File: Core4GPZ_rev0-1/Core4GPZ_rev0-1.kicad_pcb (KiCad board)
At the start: 2 copper layers, 91.4 x 109.2 mm, 41 parts, among them IC1 MAX9926UAEE_V+, M3 MountingHole_3.2mm_M3_DIN965_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, Q1 FGP3440G2-F085, Q2 FGP3440G2-F085, U1 core4, U2 MPX4250

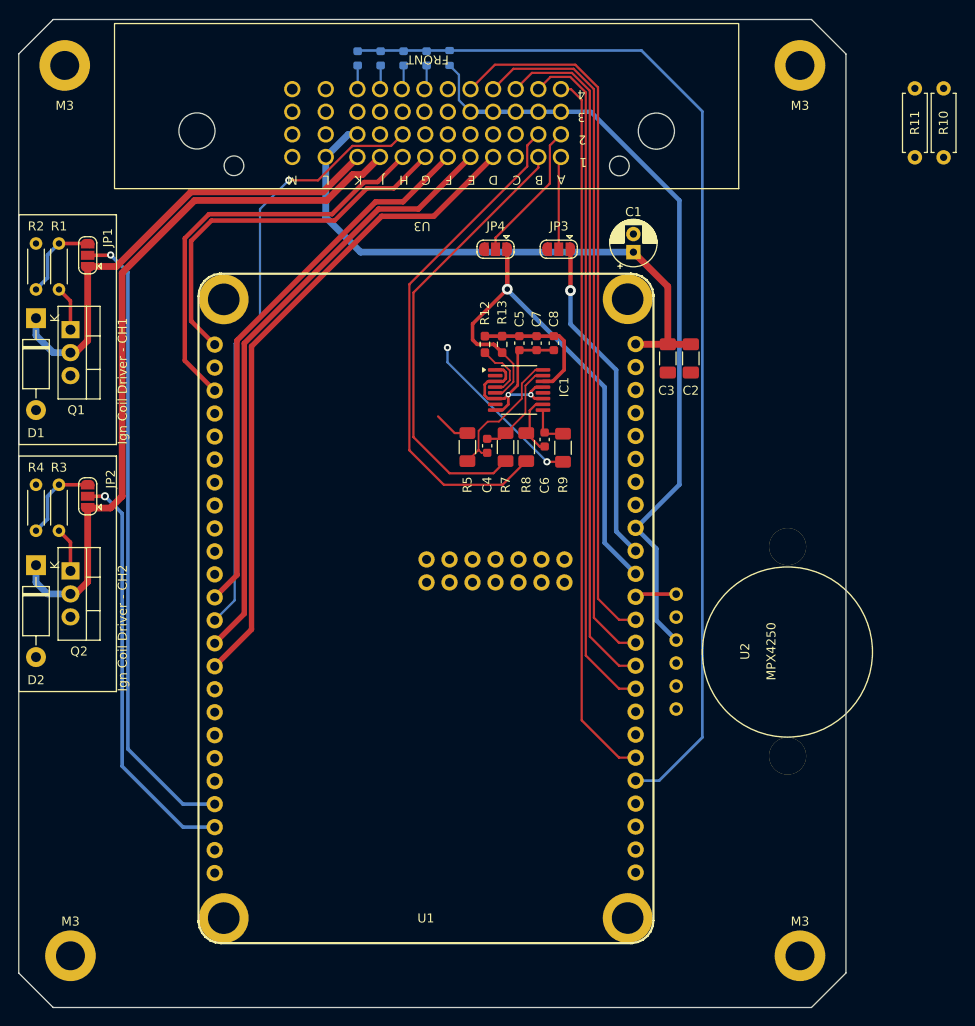
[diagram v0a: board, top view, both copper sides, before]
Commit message: Frist revision
First revision finished, optimised routing, board turned 180°.
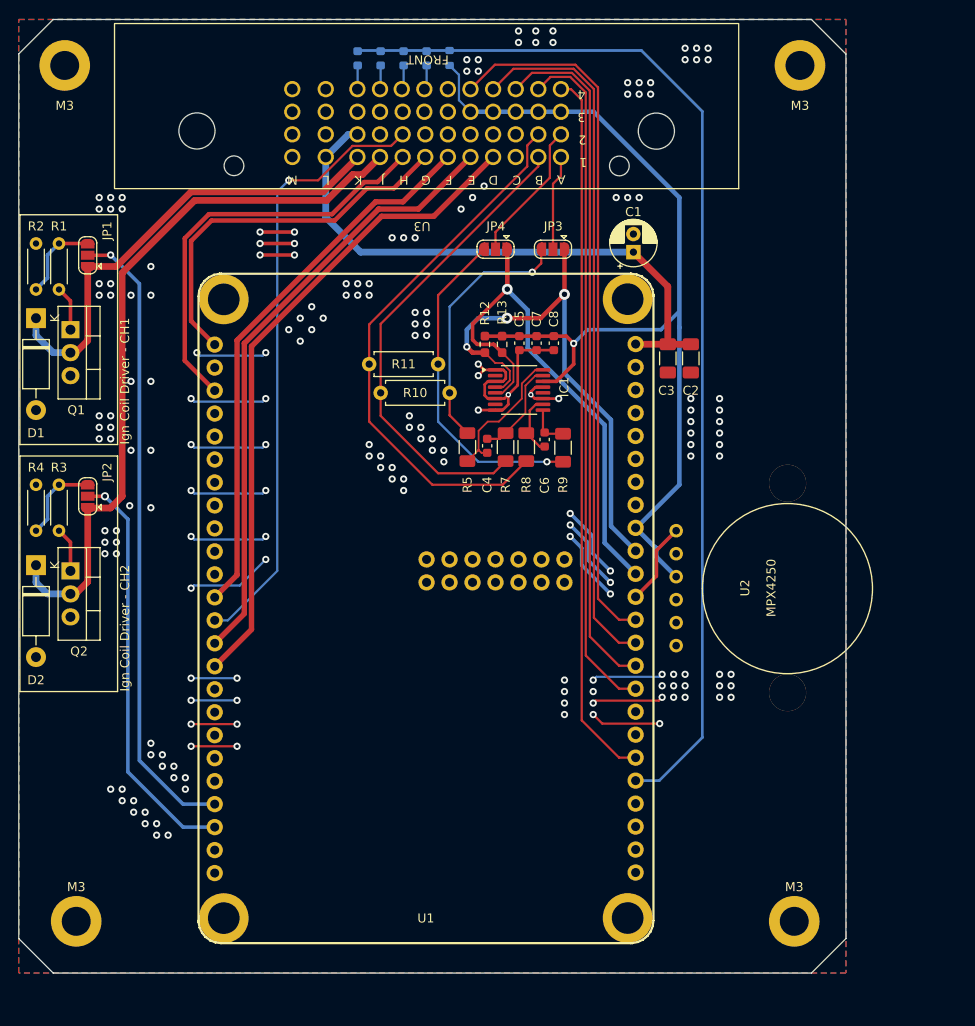
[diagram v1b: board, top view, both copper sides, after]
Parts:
- moved R10 64.1 mm to (106.7, 67.9), turned to 180 degrees
- moved R11 60.9 mm to (105.4, 64.8), turned to 180 degrees
- moved U2 7.01 mm to (131.7, 83.2)
- moved M3 3.86 mm to (65.4, 126.4)
- moved M3 3.86 mm to (144.8, 126.4)
- moved JP3 0.64 mm to (118.1, 52.1)
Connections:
- U3 pad 19: /NEUTRAL_LIGHT -> unconnected-(U3A-2J-Pad19)
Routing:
- net BIKE_GROUND: track 26.9 -> 162.5 mm, vias 2 -> 188
- net Net-(JP3-B): track 4.01 -> 28.5 mm, vias 0 -> 1
- net Net-(JP4-B): track 19.0 -> 36.8 mm, vias 2 -> 1
- net CRANK_SIGNAL: track 43.1 -> 59.9 mm, vias 1 -> 3
- net CLT_+5V: track 100.7 -> 108.7 mm, vias 0 -> 1
- net Net-(U1B-MAP_IN): track 4.60 -> 9.58 mm
- net CAM_SNSR_VR-: track 56.4 -> 60.8 mm
- net CRANK_SNSR_VR-: track 49.1 -> 52.8 mm
- net /TACHO: track 66.7 -> 67.6 mm
- net CRANK_SNSR: track 10.3 -> 10.9 mm
- added copper zone on B.Cu, net BIKE_GROUND
- added copper zone on F.Cu, net BIKE_GROUND
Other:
- board size 91.4 x 109.2 mm -> 91.4 x 105.4 mm

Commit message: Finalized ground planes
Added CORE4 pads to ground
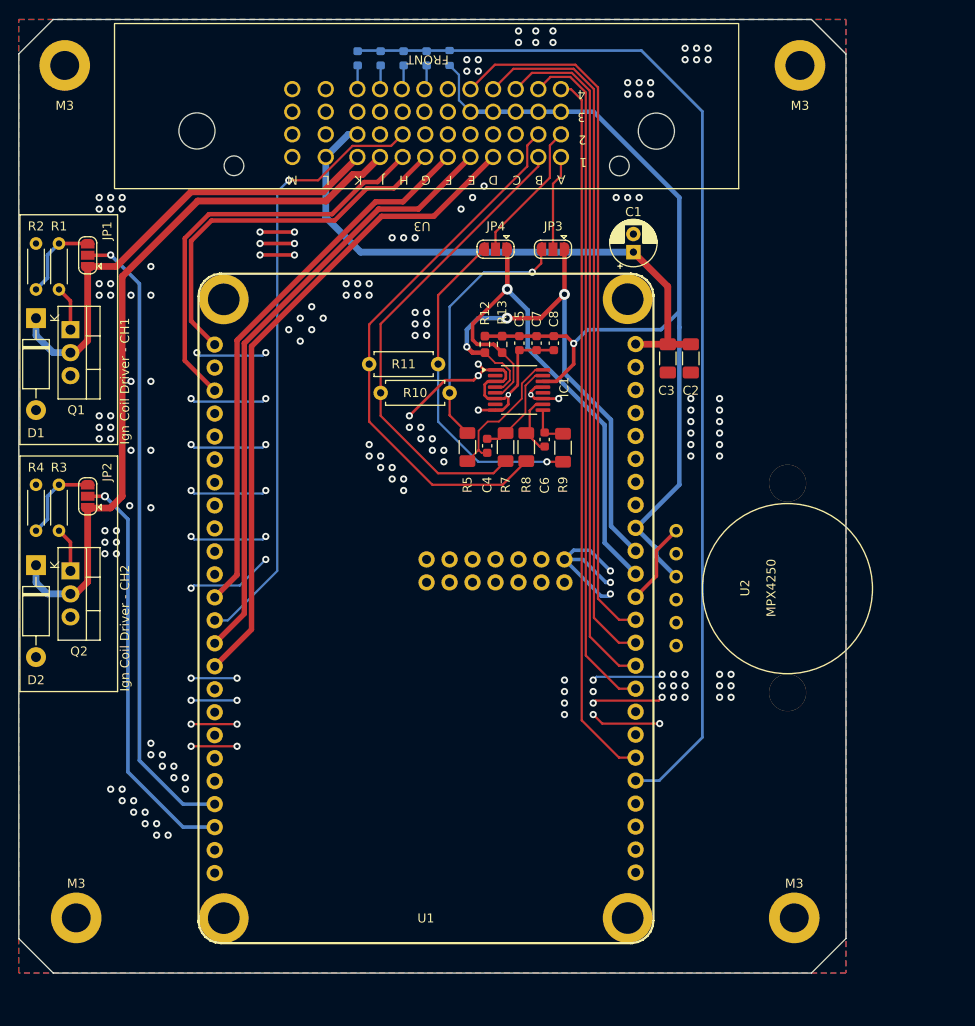
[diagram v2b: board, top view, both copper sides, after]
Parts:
- moved M3 0.38 mm to (65.4, 126.0)
- moved M3 0.38 mm to (144.8, 126.0)
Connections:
- U1 pad : (no net) -> BIKE_GROUND
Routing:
- net BIKE_GROUND: track 162.5 -> 166.9 mm, vias 188 -> 185
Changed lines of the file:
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@@
 			(layers "*.Cu" "*.Mask")
 			(remove_unused_layers no)
+			(net 2 "BIKE_GROUND")
 		)
 		(pad "" thru_hole circle
@@
 			(layers "*.Cu" "*.Mask")
 			(remove_unused_layers no)
+			(net 2 "BIKE_GROUND")
 		)
 		(pad "" thru_hole circle
@@
 			(layers "*.Cu" "*.Mask")
 			(remove_unused_layers no)
+			(net 2 "BIKE_GROUND")
 		)
 		(pad "" thru_hole circle
@@
 			(layers "*.Cu" "*.Mask")
 			(remove_unused_layers no)
+			(net 2 "BIKE_GROUND")
 		)
 		(pad "1" thru_hole circle
@@
 	(footprint "MountingHole:MountingHole_3.2mm_M3_DIN965_Pad"
 		(layer "F.Cu")
-		(at 65.405 126.365)
+		(at 65.405 125.984)
 		(descr "Mounting Hole 3.2mm, M3, DIN965")
 		(tags "mounting hole 3.2mm m3 din965")
@@
 	(footprint "MountingHole:MountingHole_3.2mm_M3_DIN965_Pad"
 		(layer "F.Cu")
-		(at 144.78 126.365)
+		(at 144.78 125.984)
 		(descr "Mounting Hole 3.2mm, M3, DIN965")
 		(tags "mounting hole 3.2mm m3 din965")
@@
 	)
 	(segment
+		(start 106.172 66.548)
+		(end 102.235 70.485)
+		(width 0.3)
+		(layer "F.Cu")
+		(net 2)
+	)
+	(segment
 		(start 123.555 104.505)
 		(end 122.555 103.505)
@@
 	)
 	(segment
+		(start 109.347 66.548)
+		(end 106.172 66.548)
+		(width 0.3)
+		(layer "F.Cu")
+		(net 2)
+	)
+	(segment
 		(start 112.88875 66.378498)
 		(end 112.592248 66.675)
@@
 	)
 	(segment
+		(start 109.855 66.04)
+		(end 109.347 66.548)
+		(width 0.3)
+		(layer "F.Cu")
+		(net 2)
+	)
+	(segment
 		(start 112.88875 65.675413)
 		(end 112.88875 66.378498)
@@
 	)
 	(via
-		(at 120.015 82.55)
-		(size 0.8)
-		(drill 0.4)
-		(layers "F.Cu" "B.Cu")
-		(free yes)
-		(net 2)
-	)
-	(via
 		(at 67.945 73.025)
 		(size 0.8)
@@
 	)
 	(via
-		(at 120.015 81.28)
-		(size 0.8)
-		(drill 0.4)
-		(layers "F.Cu" "B.Cu")
-		(free yes)
-		(net 2)
-	)
-	(via
 		(at 73.025 114.3)
 		(size 0.8)
@@
 	)
 	(via
-		(at 120.015 83.82)
-		(size 0.8)
-		(drill 0.4)
-		(layers "F.Cu" "B.Cu")
-		(free yes)
-		(net 2)
-	)
-	(via
 		(at 71.46 66.675927)
 		(size 0.8)
@@
 	)
 	(segment
+		(start 124.46 87.63)
+		(end 122.174 85.344)
+		(width 0.4)
+		(layer "B.Cu")
+		(net 2)
+	)
+	(segment
 		(start 83.485 89.235)
 		(end 78.405 89.235)
@@
 	)
 	(segment
-		(start 124.46 87.63)
-		(end 122.555 85.725)
-		(width 0.4)
+		(start 86.025 68.915)
+		(end 86.36 68.58)
+		(width 0.25)
 		(layer "B.Cu")
 		(net 2)
 	)
 	(segment
-		(start 121.92 86.36)
-		(end 121.92 84.455)
+		(start 122.174 85.344)
+		(end 120.391 85.344)
 		(width 0.4)
 		(layer "B.Cu")
@@
 	)
 	(segment
-		(start 86.025 68.915)
-		(end 86.36 68.58)
-		(width 0.25)
-		(layer "B.Cu")
-		(net 2)
-	)
-	(segment
 		(start 86.025 79.075)
 		(end 86.36 78.74)
@@
 	)
 	(segment
-		(start 79.075 63.835)
-		(end 86.025 63.835)
-		(width 0.25)
-		(layer "B.Cu")
-		(net 2)
-	)
-	(segment
-		(start 122.555 83.82)
-		(end 120.015 81.28)
+		(start 121.412 86.36)
+		(end 119.375 86.36)
 		(width 0.4)
 		(layer "B.Cu")
@@
 	)
 	(segment
-		(start 124.46 90.17)
-		(end 121.285 86.995)
-		(width 0.4)
+		(start 79.075 63.835)
+		(end 86.025 63.835)
+		(width 0.25)
 		(layer "B.Cu")
 		(net 2)
@@
 	)
 	(segment
-		(start 124.46 88.9)
-		(end 121.92 86.36)
+		(start 120.391 85.344)
+		(end 119.375 86.36)
 		(width 0.4)
 		(layer "B.Cu")
@@
 	)
 	(segment
-		(start 121.285 86.995)
-		(end 121.285 85.09)
+		(start 124.46 90.17)
+		(end 124.206 90.424)
+		(width 0.4)
+		(layer "B.Cu")
+		(net 2)
+	)
+	(segment
+		(start 123.439 90.424)
+		(end 119.375 86.36)
 		(width 0.4)
 		(layer "B.Cu")
@@
 	)
 	(segment
-		(start 122.555 85.725)
-		(end 122.555 83.82)
-		(width 0.4)
-		(layer "B.Cu")
-		(net 2)
-	)
-	(segment
-		(start 121.285 85.09)
-		(end 120.015 83.82)
+		(start 124.206 90.424)
+		(end 123.439 90.424)
 		(width 0.4)
 		(layer "B.Cu")
@@
 	)
 	(segment
+		(start 123.952 88.9)
+		(end 121.412 86.36)
+		(width 0.4)
+		(layer "B.Cu")
+		(net 2)
+	)
+	(segment
 		(start 83.185 101.935)
 		(end 78.105 101.935)
@@
 	)
 	(segment
-		(start 121.92 84.455)
-		(end 120.015 82.55)
+		(start 124.46 88.9)
+		(end 123.952 88.9)
 		(width 0.4)
 		(layer "B.Cu")
@@
 	)
 	(segment
+		(start 78.840251 46.736)
+		(end 93.037502 46.736)
+		(width 0.75)
+		(layer "F.Cu")
+		(net 9)
+	)
+	(segment
 		(start 64.77 90.17)
 		(end 65.3325 90.17)
@@
 	)
 	(segment
+		(start 70.485 79.375)
+		(end 70.485 55.091251)
+		(width 0.75)
+		(layer "F.Cu")
+		(net 9)
+	)
+	(segment
 		(start 64.5975 90.17)
 		(end 64.135 90.17)
@@
 	)
 	(segment
-		(start 78.498502 46.67)
-		(end 93.103502 46.67)
+		(start 93.037502 46.736)
+		(end 95.958502 43.815)
 		(width 0.75)
 		(layer "F.Cu")
@@
 	)
 	(segment
-		(start 93.103502 46.67)
-		(end 95.958502 43.815)
-		(width 0.75)
-		(layer "F.Cu")
-		(net 9)
-	)
-	(segment
-		(start 70.485 54.683502)
-		(end 78.498502 46.67)
-		(width 0.75)
+		(start 66.645 80.675)
+		(end 66.675 80.675)
+		(width 0.65)
 		(layer "F.Cu")
 		(net 9)
 	)
 	(segment
-		(start 70.485 79.375)
-		(end 70.485 54.683502)
+		(start 95.958502 43.815)
+		(end 97.045 43.815)
 		(width 0.75)
 		(layer "F.Cu")
@@
 	)
 	(segment
-		(start 66.645 80.675)
-		(end 66.675 80.675)
-		(width 0.65)
-		(layer "F.Cu")
-		(net 9)
-	)
-	(segment
-		(start 69.185 80.675)
-		(end 70.485 79.375)
+		(start 70.485 55.091251)
+		(end 78.840251 46.736)
 		(width 0.75)
 		(layer "F.Cu")
@@
 	)
 	(segment
-		(start 95.958502 43.815)
-		(end 97.045 43.815)
+		(start 69.185 80.675)
+		(end 70.485 79.375)
 		(width 0.75)
 		(layer "F.Cu")

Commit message: Rewied ground plane, set all SNSR+5V ref to one pin
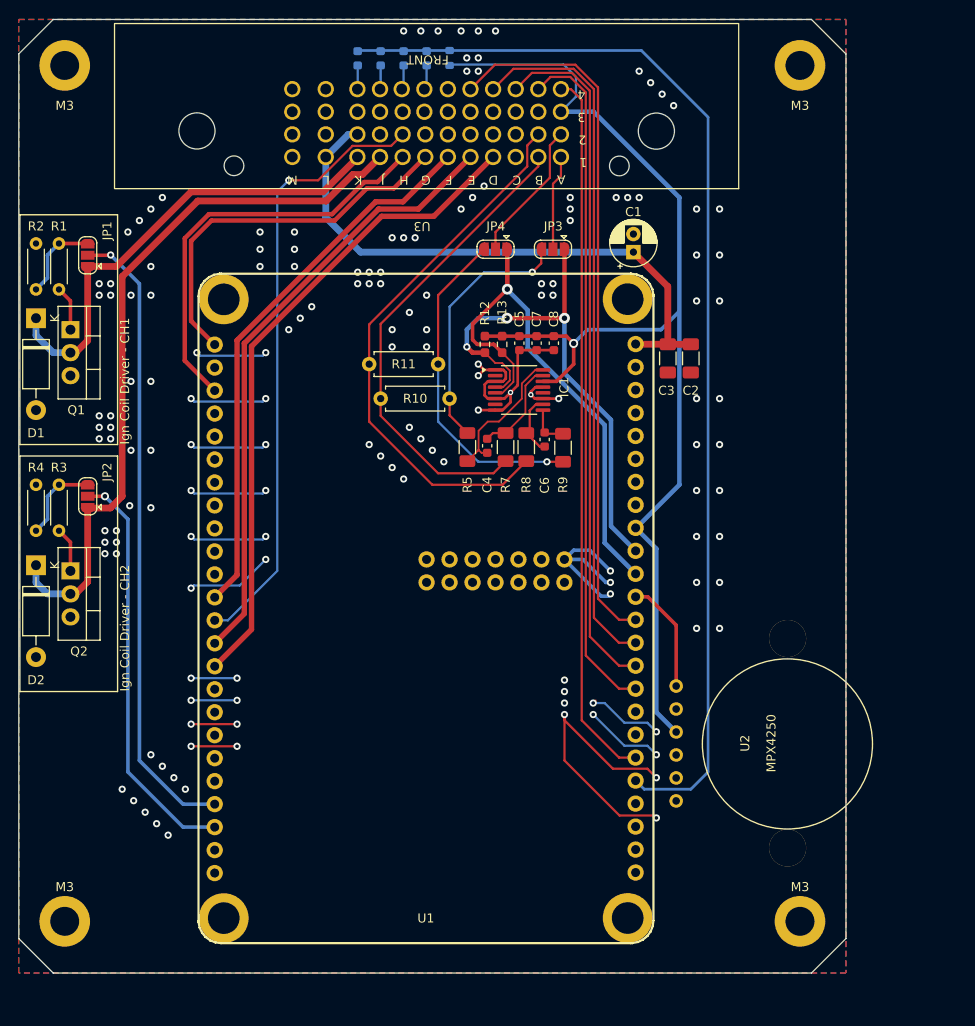
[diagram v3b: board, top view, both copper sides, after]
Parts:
- moved U2 17.2 mm to (131.7, 100.4)
- moved M3 1.33 mm to (64.1, 126.4)
- moved M3 0.74 mm to (145.4, 126.4)
- moved R10 0.64 mm to (106.7, 68.6)
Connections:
- C5 pad 1: CLT_+5V -> SNSR_+5V
- C7 pad 1: CLT_+5V -> SNSR_+5V
- C8 pad 1: CLT_+5V -> SNSR_+5V
- IC1 pad 14: CLT_+5V -> SNSR_+5V
- R12 pad 1: CLT_+5V -> SNSR_+5V
- R13 pad 1: CLT_+5V -> SNSR_+5V
- R6 pad 1: CLT_+5V -> SNSR_+5V
- U1 pad : BIKE_GROUND -> (no net)
- U1 pad 33: CLT_+5V -> SNSR_+5V
- U2 pad 3: CLT_+5V -> SNSR_+5V
- U3 pad 21: CLT_+5V -> SNSR_+5V
- U3 pad 22: CLT_+5V -> unconnected-(U3B-3B-Pad22)
- U3 pad 23: CLT_+5V -> unconnected-(U3B-3C-Pad23)
- U3 pad 24: CLT_+5V -> unconnected-(U3B-3D-Pad24)
- U3 pad 25: CLT_+5V -> unconnected-(U3B-3E-Pad25)
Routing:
- net SNSR_+5V: track 0.00 -> 128.8 mm, vias 0 -> 1
- net CLT_+5V: track 108.7 -> 0.00 mm, vias 1 -> 0
- net BIKE_GROUND: track 166.9 -> 171.6 mm, vias 185 -> 154
- net SAFE_SIGNAL: track 119.5 -> 123.4 mm
- net Net-(U1B-MAP_IN): track 9.58 -> 12.9 mm
- net CRANK_SIGNAL: track 59.9 -> 58.8 mm

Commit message: Reworked the VR conditionner
Schematic and PCB based on the Dropbear model
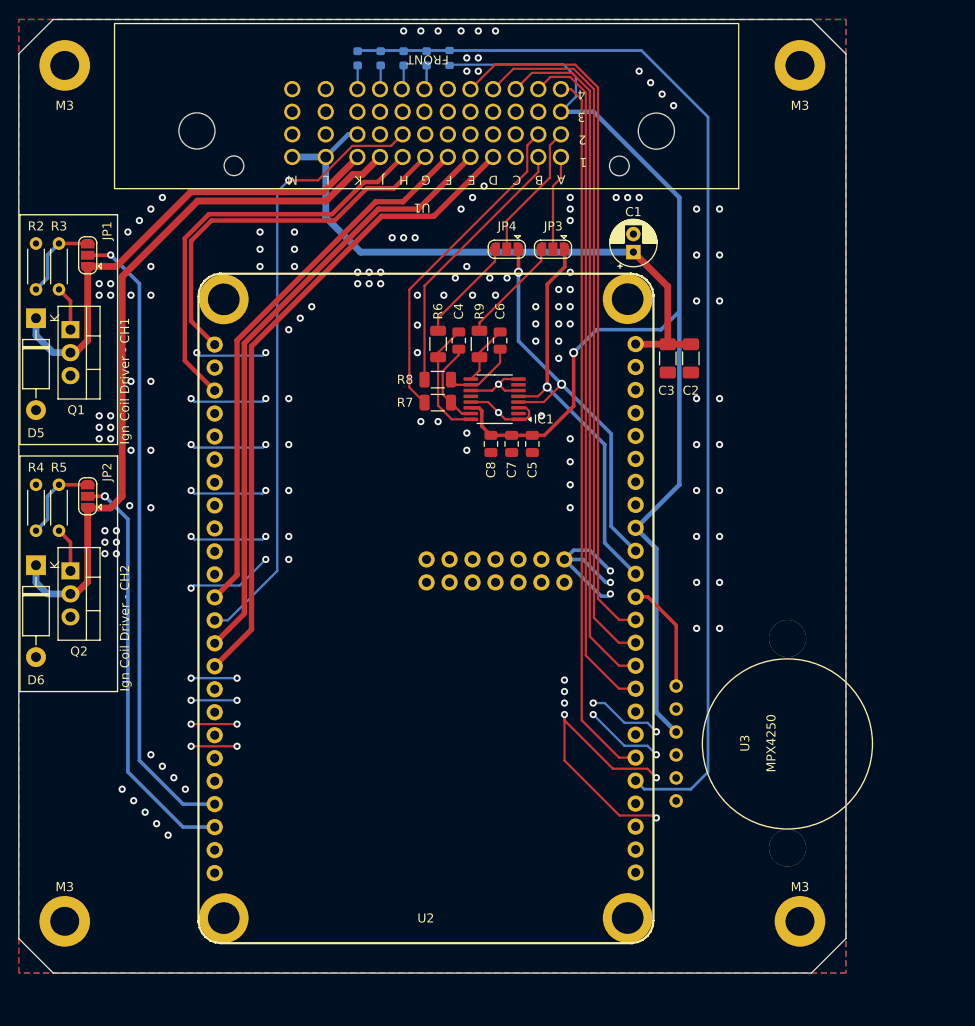
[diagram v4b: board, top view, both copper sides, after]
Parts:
- removed R10, R11: 4.7k, Resistor_THT:R_Axial_DIN0207_L6.3mm_D2.5mm_P7.62mm_Horizontal
- removed R12, R13: 1k, Resistor_SMD:R_0603_1608Metric_Pad0.98x0.95mm_HandSolder
- removed the R5 at (108.6, 73.9)
- added R6: 10k, Resistor_SMD:R_1206_3216Metric, F.Cu at (105.4, 62.5)
- C4, C6: value 1n -> 1nF; footprint Capacitor_SMD:C_0603_1608Metric -> Capacitor_SMD:C_0805_2012Metric
- C5: value 10n -> 10nF; footprint Capacitor_SMD:C_0603_1608Metric -> Capacitor_SMD:C_0805_2012Metric
- C7: value 100n -> 100nF; footprint Capacitor_SMD:C_0603_1608Metric -> Capacitor_SMD:C_0805_2012Metric
- C8: value 1u -> 1uF; footprint Capacitor_SMD:C_0603_1608Metric -> Capacitor_SMD:C_0805_2012Metric
- JP3: value Crank - VR/Hall Selector -> CAM - VR/Hall Selector
- JP4: value Cam - VR/Hall Selector -> CRANK - VR/Hall Selector
- R7, R8, R9: footprint Resistor_SMD:R_1206_3216Metric_Pad1.30x1.75mm_HandSolder -> Resistor_SMD:R_1206_3216Metric
- moved R9 14.7 mm to (110.0, 62.5)
- moved C8 13.1 mm to (111.3, 73.6)
- moved R8 12.3 mm to (105.4, 66.5), turned to 0 degrees
- moved C4 12.1 mm to (107.7, 62.2), turned to -90 degrees
- moved C6 12.0 mm to (112.3, 62.2)
- moved C7 11.5 mm to (113.5, 73.6)
- moved C5 11.2 mm to (115.8, 73.6)
- moved R7 8.96 mm to (105.4, 69.0), turned to 0 degrees
- moved IC1 2.89 mm to (111.7, 68.6), turned to 180 degrees
- moved JP4 1.24 mm to (113.0, 52.1)
- renumbered D3 to D1, D4 to D2, D5 to D3, D6 to D4, D1 to D5, D2 to D6, R6 to R1, R1 to R3, R3 to R5, U3 to U1, U1 to U2, U2 to U3
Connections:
- JP3 pad 1: CRANK_SIGNAL -> CAM_SIGNAL
- JP3 pad 2: CRANK_SNSR -> CAM_SNSR
- JP4 pad 1: CAM_SIGNAL -> CRANK_SIGNAL
- JP4 pad 2: CAM_SNSR -> CRANK_SNSR
- R7 pad 1: Net-(IC1-IN1-) -> CRANK_SNSR_VR-
- R7 pad 2: CRANK_SNSR_VR- -> Net-(IC1-IN1-)
- R8 pad 1: Net-(IC1-IN2-) -> CAM_SNSR_VR-
- R8 pad 2: CAM_SNSR_VR- -> Net-(IC1-IN2-)
- R9 pad 1: Net-(IC1-IN2+) -> Net-(JP3-B)
- R9 pad 2: Net-(JP4-B) -> Net-(IC1-IN2+)
- U1 pad 1: CRANK_SNSR -> CAM_SNSR
- U1 pad 11: CAM_SNSR -> CRANK_SNSR
- U1 pad 12: CAM_SNSR_VR- -> CRANK_SNSR_VR-
- U1 pad 2: CRANK_SNSR_VR- -> CAM_SNSR_VR-
- U1 pad 42: BIKE_GROUND -> BIKE_+12V_SWITCHED_IN
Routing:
- net CAM_SNSR_VR-: track 60.8 -> 29.9 mm
- net Net-(JP4-B): track 36.8 -> 11.6 mm, vias 1 -> 0
- net Net-(JP3-B): track 28.5 -> 11.8 mm, vias 1 -> 0
- net CRANK_SNSR_VR-: track 52.8 -> 36.4 mm
- net CAM_SIGNAL: track 59.0 -> 44.4 mm
- net CRANK_SIGNAL: track 58.8 -> 44.3 mm, vias 3 -> 2
- net BIKE_GROUND: track 171.6 -> 157.7 mm, vias 154 -> 168
- net CAM_SNSR: track 15.7 -> 10.9 mm
- net SNSR_+5V: track 128.8 -> 133.5 mm
- net CRANK_SNSR: track 10.9 -> 15.2 mm
- net BIKE_+12V_SWITCHED_IN: track 64.7 -> 68.4 mm
- net Net-(IC1-IN1+): track 16.0 -> 13.3 mm
- net Net-(IC1-IN2+): track 4.64 -> 6.55 mm
- net Net-(IC1-IN2-): track 7.05 -> 8.19 mm
- net Net-(IC1-IN1-): track 10.8 -> 9.72 mm
